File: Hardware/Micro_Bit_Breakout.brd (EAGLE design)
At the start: 68.6 x 22.9 mm, 13 parts, among them J1 EDGE-80PTH-RA, J2 M22PTH

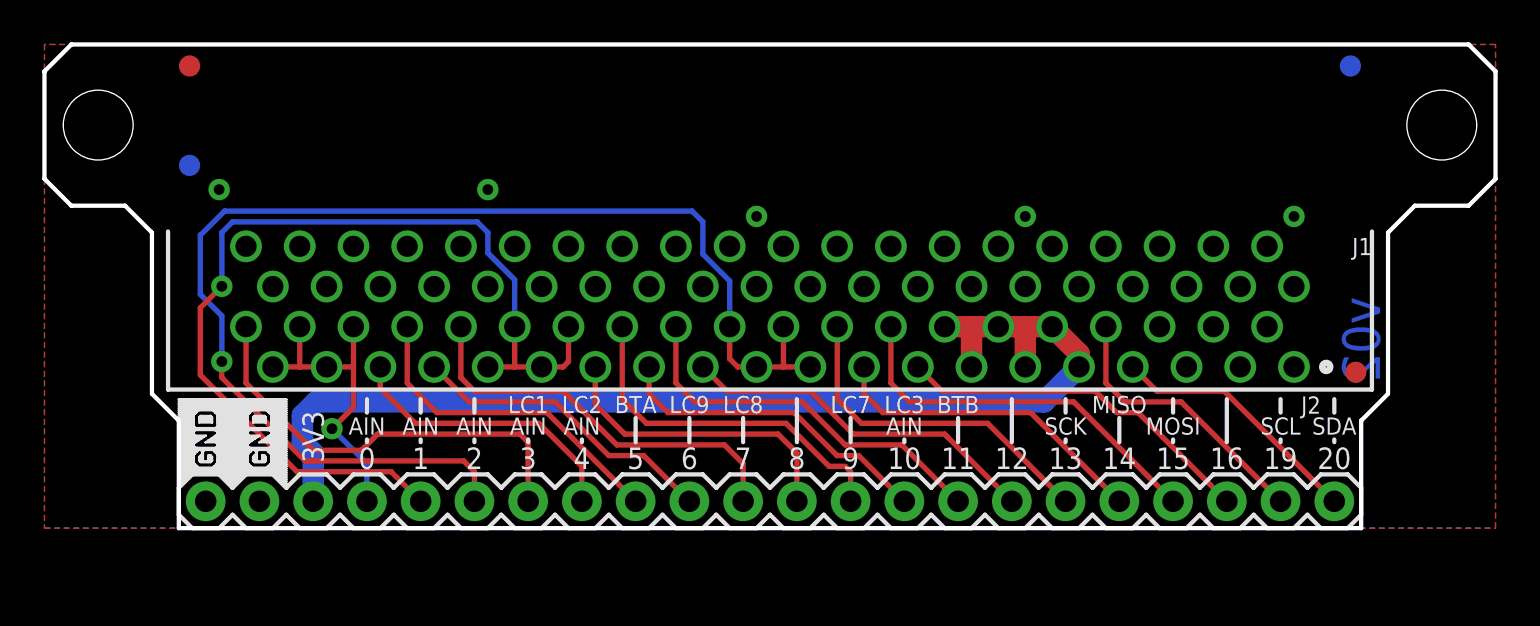
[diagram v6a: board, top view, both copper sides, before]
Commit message: v03
-Replaced micro:bit connector with SMD version
-Replaced silk with buzzard labels
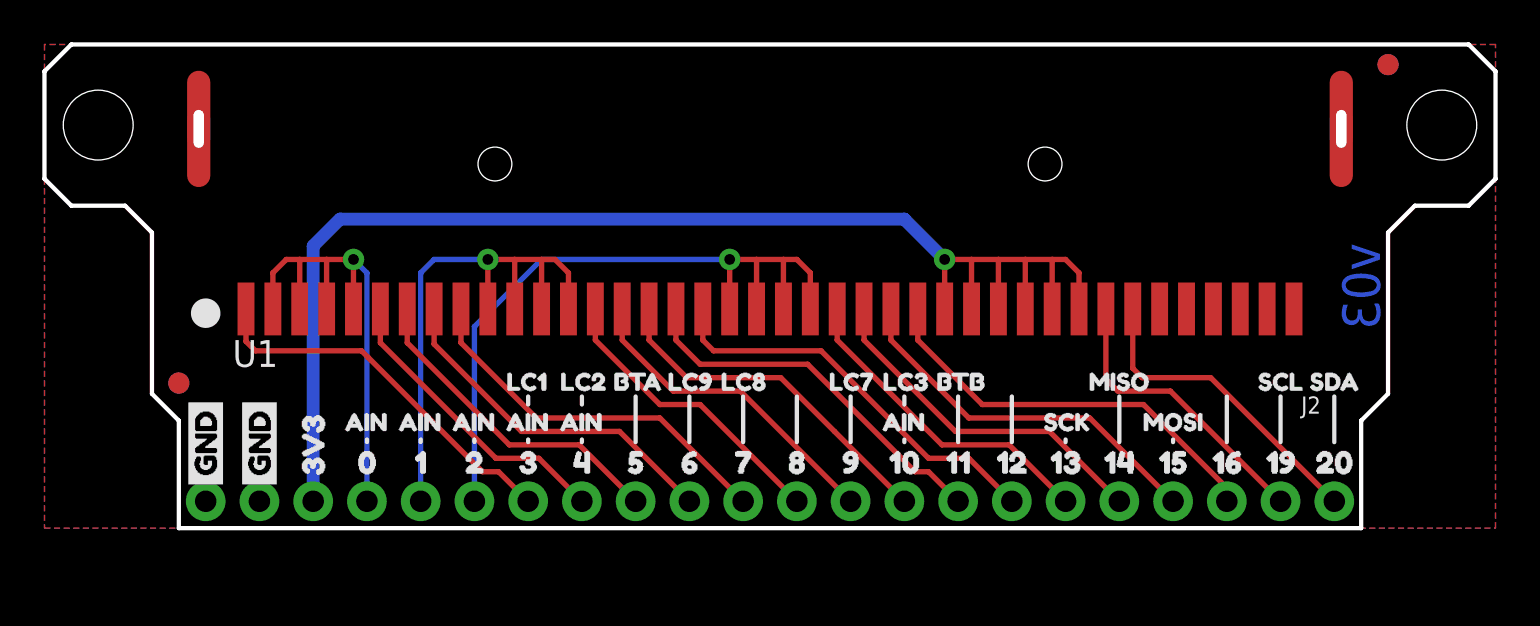
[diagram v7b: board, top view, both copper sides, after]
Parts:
- removed J1: EDGE-80PTH-RA, local_lib:VEC-127-080-R
- added U$10: (no value), buzzard_labels(1):10#AIN#LC312
- added U$11: (no value), buzzard_labels(1):9#LC711
- added U$12: (no value), buzzard_labels(1):810
- added U$13: (no value), buzzard_labels(1):7#LC89
- added U$14: (no value), buzzard_labels(1):6#LC98
- added U$15: (no value), buzzard_labels(1):5#BTA7
- added U$16: (no value), buzzard_labels(1):4#AIN#LC26
- added U$17: (no value), buzzard_labels(1):3#AIN#LC15
- added U$18: (no value), buzzard_labels(1):2#AIN4
- added U$19: (no value), buzzard_labels(1):1#AIN3
- added U$20: (no value), buzzard_labels(1):0#AIN2
- added U$21: (no value), buzzard_labels(1):3V31
- added U$22, U$23: (no value), buzzard_labels(1):GND0
- added U$24: (no value), buzzard_labels(4):GND0
- added U$25: (no value), buzzard_labels(3):MICRO#BIT_BREAKOUT0
- added U$26: (no value), buzzard_labels(4):3V31
- added U$27: (no value), buzzard_labels(4):02
- added U$28: (no value), buzzard_labels(4):13
- added U$29: (no value), buzzard_labels(4):24
- added U$3: (no value), buzzard_labels(1):19#SCL19
- added U$30: (no value), buzzard_labels(4):35
- added U$31: (no value), buzzard_labels(4):46
- added U$32: (no value), buzzard_labels(4):57
- added U$33: (no value), buzzard_labels(4):68
- added U$34: (no value), buzzard_labels(4):79
- added U$35: (no value), buzzard_labels(4):810
- added U$36: (no value), buzzard_labels(4):911
- added U$37: (no value), buzzard_labels(4):1012
- added U$38: (no value), buzzard_labels(4):1113
- added U$39: (no value), buzzard_labels(4):1214
- added U$4: (no value), buzzard_labels(1):1618
- added U$40: (no value), buzzard_labels(4):1315
- added U$41: (no value), buzzard_labels(4):1416
- added U$42: (no value), buzzard_labels(4):1517
- added U$43: (no value), buzzard_labels(4):1618
- added U$44: (no value), buzzard_labels(4):1919
- added U$45: (no value), buzzard_labels(4):2020
- added U$46, U$47, U$48, U$49, U$50, U$51: (no value), buzzard_labels(7):AIN0
- added U$5: (no value), buzzard_labels(1):15#MOSI17
- added U$52: (no value), buzzard_labels(7):LC11
- added U$53: (no value), buzzard_labels(7):LC22
- added U$54: (no value), buzzard_labels(7):BTA3
- added U$55: (no value), buzzard_labels(7):LC95
- added U$56: (no value), buzzard_labels(7):LC86
- added U$57: (no value), buzzard_labels(7):LC77
- added U$58: (no value), buzzard_labels(7):LC38
- added U$59: (no value), buzzard_labels(7):BTB4
- added U$6: (no value), buzzard_labels(1):14#MISO16
- added U$60: (no value), buzzard_labels(7):SCK9
- added U$61: (no value), buzzard_labels(7):MISO10
- added U$62: (no value), buzzard_labels(7):MOSI11
- added U$63: (no value), buzzard_labels(7):SCL12
- added U$64: (no value), buzzard_labels(7):SDA13
- added U$7: (no value), buzzard_labels(1):13#SCK15
- added U$8: (no value), buzzard_labels(1):1214
- added U$9: (no value), buzzard_labels(1):11#BTB13
- added U1: micro:bit, SparkFun-Connectors:MICRO:BIT-RA_SMD
- J2: value M22PTH -> CONN_22_NOSILK; device local_lib:1X22 -> SparkFun-Connectors:1X22_NOSILK
- LOGO3: value OSHW-LOGOS -> OSHW-LOGOM; device SparkFun-Aesthetics:OSHW-LOGO-S -> SparkFun-Aesthetics:OSHW-LOGO-M
- U$1: device negasilk:NEGASILK_MICRO_BIT_BREAKOUT -> buzzard_labels(4):GND0
- U$2: device negasilk:NEGASILK_MICRO_BIT_BREAKOUT -> buzzard_labels(1):20#SDA20
- moved FD3 57.4 mm to (6.35, 6.86)
- moved FD4 56.8 mm to (63.5, 21.9)
- moved U$2 49.5 mm to (61.0, 1.52), turned to 90 degrees
- moved LOGO2 20.1 mm to (40.2, 17.0)
- moved FD1 15.0 mm to (6.35, 6.86)
- moved FD2 14.6 mm to (63.5, 21.9)
- moved FRAME1 12.8 mm to (1.27, -24.1)
- moved LOGO3 3.21 mm to (11.7, 16.0)
- moved U$1 1.31 mm to (7.62, 1.59), turned to 90 degrees
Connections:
- net 0: now also U1.P$2, U1.P$3, U1.P$4, U1.P$5; no longer J1.A36, J1.A37, J1.A38, J1.A39
- net 1: now also U1.P$10, U1.P$11, U1.P$12, U1.P$13; no longer J1.A28, J1.A29, J1.A30, J1.A31
- net 10: now also U1.P$16; no longer J1.A25
- net 11: now also U1.P$17; no longer J1.A24
- net 12: now also U1.P$18; no longer J1.A23
- net 13: now also U1.P$23; no longer J1.A18
- net 14: now also U1.P$24; no longer J1.A17
- net 15: now also U1.P$25; no longer J1.A16
- net 16: now also U1.P$26; no longer J1.A15
- net 19: now also U1.P$33; no longer J1.A8
- net 2: now also U1.P$19, U1.P$20, U1.P$21, U1.P$22; no longer J1.A19, J1.A20, J1.A21, J1.A22
- net 20: now also U1.P$34; no longer J1.A7
- net 3: now also U1.P$1; no longer J1.A40
- net 3.3V: now also U1.P$27, U1.P$28, U1.P$29, U1.P$30, U1.P$31, U1.P$32; no longer J1.A10, J1.A11, J1.A12, J1.A13, J1.A14, J1.A9
- net 4: now also U1.P$6; no longer J1.A35
- net 5: now also U1.P$7; no longer J1.A34
- net 6: now also U1.P$8; no longer J1.A33
- net 7: now also U1.P$9; no longer J1.A32
- net 8: now also U1.P$14; no longer J1.A27
- net 9: now also U1.P$15; no longer J1.A26
- net GND: now also U1.P$35, U1.P$36, U1.P$37, U1.P$38, U1.P$39, U1.P$40; no longer J1.A1, J1.A2, J1.A3, J1.A4, J1.A5, J1.A6
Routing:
- net 2: track 59.6 -> 34.4 mm
- net 1: track 45.5 -> 27.0 mm
- net 3.3V: track 53.3 -> 63.2 mm, vias 0 -> 1
- net 0: track 15.1 -> 24.5 mm
- net 20: track 12.2 -> 14.9 mm
- net 3: track 20.6 -> 18.0 mm
- net 16: track 17.2 -> 19.6 mm
- net 6: track 14.7 -> 16.8 mm
- net 12: track 17.2 -> 19.2 mm
- net 9: track 17.0 -> 15.4 mm
- net 10: track 15.4 -> 16.7 mm
- net 14: track 15.4 -> 16.7 mm
- net 7: track 19.2 -> 18.0 mm
- net 13: track 16.2 -> 15.4 mm
- net 19: track 13.2 -> 14.0 mm
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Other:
- board text added: "Revised by: Alex Wende"
- board text added: "v03"
- board text removed: "* All dimensions are in inches"
- board text removed: "0"
- board text removed: "1"
- board text removed: "10"
- board text removed: "11"
- board text removed: "12"
- board text removed: "13"
- board text removed: "14"
- board text removed: "15"
- board text removed: "16"
- board text removed: "19"
- board text removed: "2"
- board text removed: "20"
- board text removed: "3"
- board text removed: "3V3"
- board text removed: "4"
- board text removed: "5"
- board text removed: "6"
- board text removed: "7"
- board text removed: "8"
- board text removed: "9"
- board text removed: "AIN"
- board text removed: "BTA"
- board text removed: "BTB"
- board text removed: "LC1"
- board text removed: "LC2"
- board text removed: "LC3"
- board text removed: "LC7"
- board text removed: "LC8"
- board text removed: "LC9"
- board text removed: "MISO"
- board text removed: "MOSI"
- board text removed: "Micro Bit Breakout"
- board text removed: "SCK"
- board text removed: "SCL"
- board text removed: "SDA"
- board text removed: "v02"
